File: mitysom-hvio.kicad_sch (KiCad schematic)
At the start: 34 parts, among them J1 Plug_Samtec_SEAM-50-02.0-L-08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, U1 TXS0102DQER, U48 TCA39306_VSSOP, U50 TCA39306_VSSOP, U501 TXU0304BQAR

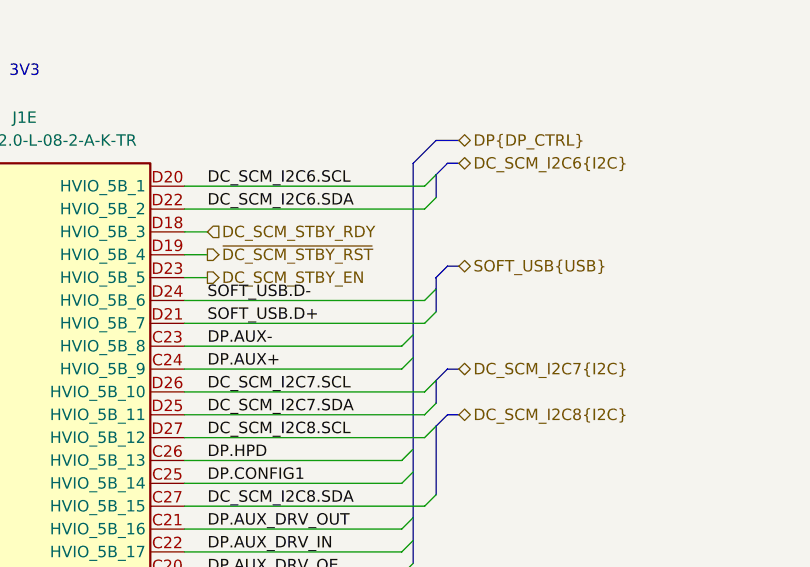
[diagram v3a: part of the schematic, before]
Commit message: [#100707] Connect power and low speed signals
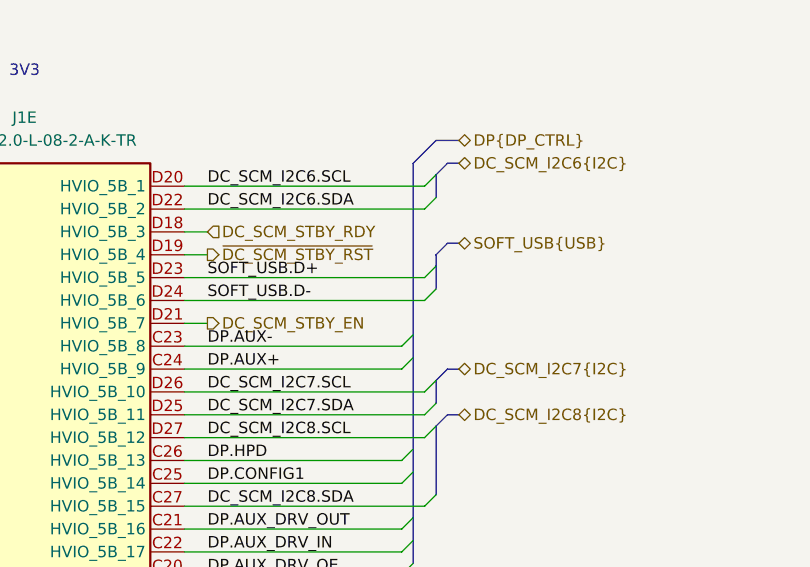
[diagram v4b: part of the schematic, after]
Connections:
- net DC_SCM_STBY_EN: now also J1.D21 (HVIO_5B_7); no longer J1.D23 (HVIO_5B_5)
- net SOFT_USB.D+: now also J1.D23 (HVIO_5B_5); no longer J1.D21 (HVIO_5B_7)
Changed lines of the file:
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@@
 	)
 	(bus_entry
+		(at 195.58 224.79)
+		(size -1.27 1.27)
+		(stroke
+			(width 0)
+			(type default)
+		)
+	)
+	(bus_entry
 		(at 210.82 102.87)
 		(size -1.27 -1.27)
@@
 	)
 	(bus_entry
-		(at 195.58 227.33)
-		(size -1.27 1.27)
-		(stroke
-			(width 0)
-			(type default)
-		)
-	)
-	(bus_entry
 		(at 238.76 179.07)
 		(size -1.27 1.27)
@@
 	)
 	(bus_entry
+		(at 195.58 222.25)
+		(size -1.27 1.27)
+		(stroke
+			(width 0)
+			(type default)
+		)
+	)
+	(bus_entry
 		(at 198.12 62.23)
 		(size -1.27 1.27)
@@
 	)
 	(bus_entry
-		(at 195.58 224.79)
-		(size -1.27 1.27)
-		(stroke
-			(width 0)
-			(type default)
-		)
-	)
-	(bus_entry
 		(at 92.71 257.81)
 		(size 1.27 1.27)
@@
 	(wire
 		(pts
-			(xy 167.64 228.6) (xy 194.31 228.6)
-		)
-		(stroke
-			(width 0)
-			(type default)
-		)
-	)
-	(wire
-		(pts
 			(xy 134.62 133.35) (xy 119.38 133.35)
 		)
@@
 	(bus
 		(pts
-			(xy 195.58 224.79) (xy 195.58 227.33)
-		)
-		(stroke
-			(width 0)
-			(type default)
-		)
-	)
-	(bus
-		(pts
 			(xy 104.14 95.25) (xy 104.14 97.79)
 		)
@@
 		)
 	)
+	(bus
+		(pts
+			(xy 198.12 219.71) (xy 196.85 219.71)
+		)
+		(stroke
+			(width 0)
+			(type default)
+		)
+	)
 	(wire
 		(pts
@@
 		)
 	)
+	(bus
+		(pts
+			(xy 195.58 220.98) (xy 195.58 222.25)
+		)
+		(stroke
+			(width 0)
+			(type default)
+		)
+	)
 	(wire
 		(pts
@@
 		)
 	)
-	(bus
-		(pts
-			(xy 198.12 222.25) (xy 196.85 222.25)
-		)
-		(stroke
-			(width 0)
-			(type default)
-		)
-	)
 	(wire
 		(pts
@@
 		)
 	)
-	(wire
+	(bus
 		(pts
-			(xy 170.18 223.52) (xy 167.64 223.52)
+			(xy 195.58 222.25) (xy 195.58 224.79)
 		)
 		(stroke
@@
 		)
 	)
-	(bus
-		(pts
-			(xy 195.58 223.52) (xy 195.58 224.79)
-		)
-		(stroke
-			(width 0)
-			(type default)
-		)
-	)
 	(wire
 		(pts
@@
 		)
 	)
+	(bus
+		(pts
+			(xy 196.85 219.71) (xy 195.58 220.98)
+		)
+		(stroke
+			(width 0)
+			(type default)
+		)
+	)
 	(wire
 		(pts
@@
 	(wire
 		(pts
+			(xy 167.64 223.52) (xy 194.31 223.52)
+		)
+		(stroke
+			(width 0)
+			(type default)
+		)
+	)
+	(wire
+		(pts
 			(xy 302.26 181.61) (xy 304.8 181.61)
 		)
@@
 	(bus
 		(pts
-			(xy 196.85 222.25) (xy 195.58 223.52)
-		)
-		(stroke
-			(width 0)
-			(type default)
-		)
-	)
-	(bus
-		(pts
 			(xy 91.44 256.54) (xy 92.71 257.81)
 		)
@@
 		)
 	)
+	(wire
+		(pts
+			(xy 170.18 228.6) (xy 167.64 228.6)
+		)
+		(stroke
+			(width 0)
+			(type default)
+		)
+	)
 	(label "DC_SCM_SPI_SCMCNTRL.~{CS0}"
 		(at 170.18 63.5 0)
@@
 		)
 	)
-	(label "SOFT_USB.D+"
-		(at 170.18 228.6 0)
-		(effects
-			(font
-				(size 1.27 1.27)
-			)
-			(justify left bottom)
-		)
-	)
 	(label "DC_SCM_NC-SI.CRS_DV"
 		(at 106.68 99.06 0)
@@
 		)
 	)
+	(label "SOFT_USB.D+"
+		(at 170.18 223.52 0)
+		(effects
+			(font
+				(size 1.27 1.27)
+			)
+			(justify left bottom)
+		)
+	)
 	(label "DC_SCM_ESPI.IO3"
 		(at 106.68 76.2 0)
@@
 		)
 	)
+	(hierarchical_label "DC_SCM_STBY_EN"
+		(shape output)
+		(at 170.18 228.6 0)
+		(effects
+			(font
+				(size 1.27 1.27)
+			)
+			(justify left)
+		)
+	)
 	(hierarchical_label "~{PECI_ALERT}"
 		(shape input)
@@
 		)
 	)
+	(hierarchical_label "SOFT_USB{USB}"
+		(shape bidirectional)
+		(at 198.12 219.71 0)
+		(effects
+			(font
+				(size 1.27 1.27)
+			)
+			(justify left)
+		)
+	)
 	(hierarchical_label "PCIE_RST_B"
 		(shape input)
@@
 		)
 	)
-	(hierarchical_label "SOFT_USB{USB}"
-		(shape bidirectional)
-		(at 198.12 222.25 0)
-		(effects
-			(font
-				(size 1.27 1.27)
-			)
-			(justify left)
-		)
-	)
 	(hierarchical_label "PCIE_PWR_EN"
 		(shape input)
@@
 		)
 	)
-	(hierarchical_label "DC_SCM_STBY_EN"
-		(shape output)
-		(at 170.18 223.52 0)
-		(effects
-			(font
-				(size 1.27 1.27)
-			)
-			(justify left)
-		)
-	)
 	(hierarchical_label "DC_SCM_SPI_SCMCNTRL{SPI}"
 		(shape bidirectional)
@@
 		(length 2.54)
 		(shape round)
-		(at 195.58 226.06 270)
+		(at 195.58 223.52 270)
 		(effects
 			(font
@@
 		)
 		(property "Netclass" "90Ohm-diff"
-			(at 199.39 226.06 0)
+			(at 199.39 223.52 0)
 			(show_name no)
 			(do_not_autoplace no)
@@
 		)
 		(property "Component Class" ""
-			(at 394.97 102.87 0)
+			(at 394.97 100.33 0)
 			(show_name no)
 			(do_not_autoplace no)

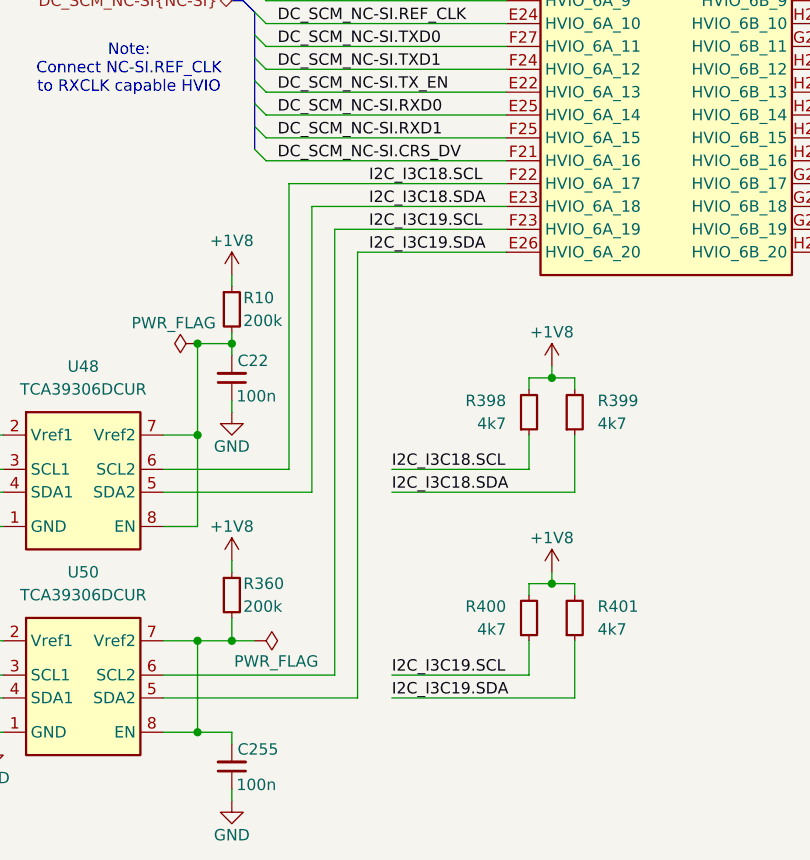
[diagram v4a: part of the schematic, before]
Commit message: [#101095] Swap I2C lines on HVIO
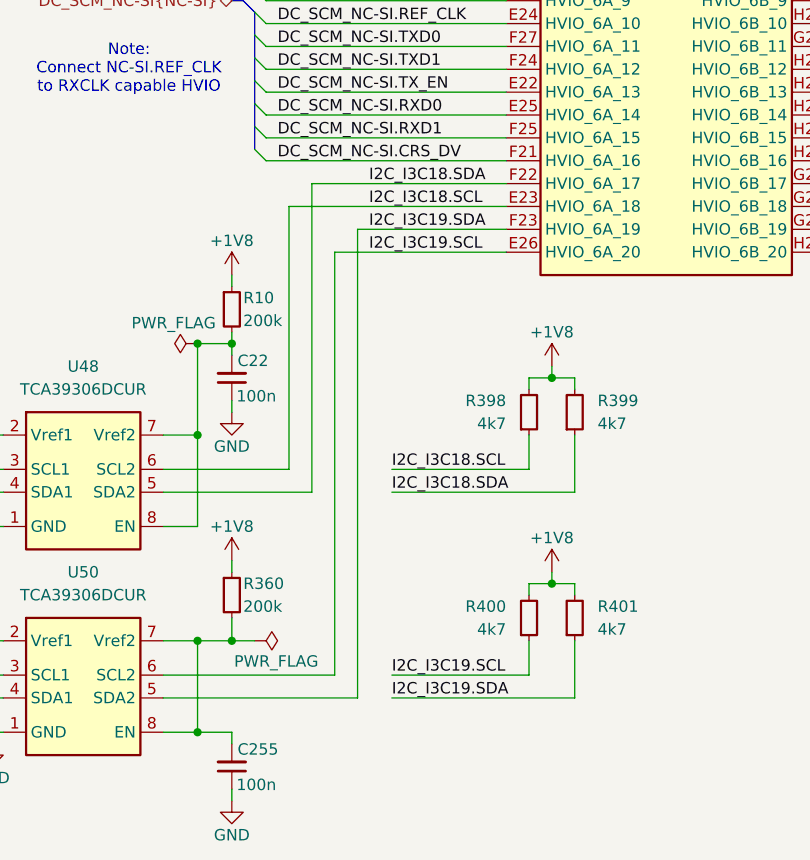
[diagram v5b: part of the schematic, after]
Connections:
- net I2C_I3C18.SCL: now also J1.E23 (HVIO_6A_18); no longer J1.F22 (HVIO_6A_17)
- net I2C_I3C18.SDA: now also J1.F22 (HVIO_6A_17); no longer J1.E23 (HVIO_6A_18)
- net I2C_I3C19.SCL: now also J1.E26 (HVIO_6A_20); no longer J1.F23 (HVIO_6A_19)
- net I2C_I3C19.SDA: now also J1.F23 (HVIO_6A_19); no longer J1.E26 (HVIO_6A_20)
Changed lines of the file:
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@@
 		)
 	)
-	(wire
-		(pts
-			(xy 110.49 104.14) (xy 132.08 104.14)
-		)
-		(stroke
-			(width 0)
-			(type default)
-		)
-	)
 	(bus
 		(pts
@@
 	(wire
 		(pts
+			(xy 110.49 101.6) (xy 110.49 135.89)
+		)
+		(stroke
+			(width 0)
+			(type default)
+		)
+	)
+	(wire
+		(pts
 			(xy 238.76 161.29) (xy 266.7 161.29)
 		)
@@
 	(wire
 		(pts
-			(xy 115.57 109.22) (xy 132.08 109.22)
+			(xy 113.03 109.22) (xy 132.08 109.22)
 		)
 		(stroke
@@
 	(wire
 		(pts
-			(xy 113.03 106.68) (xy 132.08 106.68)
+			(xy 115.57 106.68) (xy 132.08 106.68)
 		)
 		(stroke
@@
 	(wire
 		(pts
-			(xy 107.95 101.6) (xy 132.08 101.6)
-		)
-		(stroke
-			(width 0)
-			(type default)
-		)
-	)
-	(wire
-		(pts
 			(xy 167.64 88.9) (xy 209.55 88.9)
 		)
@@
 	(wire
 		(pts
-			(xy 110.49 104.14) (xy 110.49 135.89)
-		)
-		(stroke
-			(width 0)
-			(type default)
-		)
-	)
-	(wire
-		(pts
 			(xy 134.62 146.05) (xy 134.62 147.32)
 		)
@@
 	(wire
 		(pts
-			(xy 115.57 109.22) (xy 115.57 158.75)
-		)
-		(stroke
-			(width 0)
-			(type default)
-		)
-	)
-	(wire
-		(pts
 			(xy 302.26 179.07) (xy 304.8 179.07)
 		)
@@
 	(wire
 		(pts
+			(xy 113.03 156.21) (xy 113.03 109.22)
+		)
+		(stroke
+			(width 0)
+			(type default)
+		)
+	)
+	(wire
+		(pts
 			(xy 105.41 76.2) (xy 132.08 76.2)
 		)
@@
 	(wire
 		(pts
-			(xy 113.03 106.68) (xy 113.03 156.21)
-		)
-		(stroke
-			(width 0)
-			(type default)
-		)
-	)
-	(wire
-		(pts
 			(xy 93.98 261.62) (xy 132.08 261.62)
 		)
@@
 	(wire
 		(pts
+			(xy 115.57 106.68) (xy 115.57 158.75)
+		)
+		(stroke
+			(width 0)
+			(type default)
+		)
+	)
+	(wire
+		(pts
 			(xy 129.54 236.22) (xy 132.08 236.22)
 		)
@@
 	(wire
 		(pts
+			(xy 110.49 101.6) (xy 132.08 101.6)
+		)
+		(stroke
+			(width 0)
+			(type default)
+		)
+	)
+	(wire
+		(pts
 			(xy 238.76 146.05) (xy 266.7 146.05)
 		)
@@
 	(wire
 		(pts
-			(xy 107.95 101.6) (xy 107.95 133.35)
+			(xy 107.95 133.35) (xy 107.95 104.14)
 		)
 		(stroke
@@
 		)
 	)
+	(wire
+		(pts
+			(xy 107.95 104.14) (xy 132.08 104.14)
+		)
+		(stroke
+			(width 0)
+			(type default)
+		)
+	)
 	(bus
 		(pts
@@
 		)
 	)
+	(label "I2C_I3C18.SCL"
+		(at 116.84 104.14 0)
+		(effects
+			(font
+				(size 1.27 1.27)
+			)
+			(justify left bottom)
+		)
+	)
 	(label "DC_SCM_NC-SI.CRS_DV"
 		(at 106.68 99.06 0)
@@
 	)
 	(label "I2C_I3C19.SDA"
-		(at 116.84 109.22 0)
+		(at 119.38 158.75 0)
 		(effects
 			(font
@@
 		)
 	)
-	(label "I2C_I3C18.SDA"
-		(at 119.38 135.89 0)
-		(effects
-			(font
-				(size 1.27 1.27)
-			)
-			(justify left bottom)
-		)
-	)
-	(label "I2C_I3C18.SDA"
-		(at 116.84 104.14 0)
-		(effects
-			(font
-				(size 1.27 1.27)
-			)
-			(justify left bottom)
-		)
-	)
 	(label "GbE_TXD3"
 		(at 168.91 96.52 0)
@@
 		)
 	)
-	(label "I2C_I3C19.SCL"
-		(at 116.84 106.68 0)
-		(effects
-			(font
-				(size 1.27 1.27)
-			)
-			(justify left bottom)
-		)
-	)
 	(label "DC_SCM_NC-SI.RXD1"
 		(at 106.68 96.52 0)
@@
 		)
 	)
-	(label "I2C_I3C19.SCL"
-		(at 119.38 156.21 0)
-		(effects
-			(font
-				(size 1.27 1.27)
-			)
-			(justify left bottom)
-		)
-	)
 	(label "DP.CONFIG1"
 		(at 170.18 246.38 0)
@@
 		)
 	)
+	(label "I2C_I3C19.SDA"
+		(at 116.84 106.68 0)
+		(effects
+			(font
+				(size 1.27 1.27)
+			)
+			(justify left bottom)
+		)
+	)
 	(label "DC_SCM_I2C9.SDA"
 		(at 170.18 261.62 0)
@@
 		)
 	)
-	(label "I2C_I3C19.SDA"
-		(at 119.38 158.75 0)
+	(label "I2C_I3C18.SDA"
+		(at 116.84 101.6 0)
+		(effects
+			(font
+				(size 1.27 1.27)
+			)
+			(justify left bottom)
+		)
+	)
+	(label "I2C_I3C18.SCL"
+		(at 119.38 133.35 0)
+		(effects
+			(font
+				(size 1.27 1.27)
+			)
+			(justify left bottom)
+		)
+	)
+	(label "I2C_I3C18.SDA"
+		(at 119.38 135.89 0)
 		(effects
 			(font
@@
 		)
 	)
-	(label "I2C_I3C18.SCL"
-		(at 119.38 133.35 0)
-		(effects
-			(font
-				(size 1.27 1.27)
-			)
-			(justify left bottom)
-		)
-	)
 	(label "UART_1V8_TX"
 		(at 170.18 73.66 0)
@@
 		)
 	)
+	(label "I2C_I3C19.SCL"
+		(at 116.84 109.22 0)
+		(effects
+			(font
+				(size 1.27 1.27)
+			)
+			(justify left bottom)
+		)
+	)
 	(label "SOM.IO2"
 		(at 240.03 173.99 0)
@@
 		)
 	)
-	(label "I2C_I3C18.SCL"
-		(at 116.84 101.6 0)
-		(effects
-			(font
-				(size 1.27 1.27)
-			)
-			(justify left bottom)
-		)
-	)
 	(label "DC_SCM_NC-SI.REF_CLK"
 		(at 106.68 83.82 0)
@@
 		(effects
 			(font
+				(size 1.27 1.27)
+			)
+			(justify left bottom)
+		)
+	)
+	(label "I2C_I3C19.SCL"
+		(at 119.38 156.21 0)
+		(effects
+			(font

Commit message: [#101340] Update JTAG TRST divider
Re-use 10k/12k values from other sheets
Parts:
- R502: value R_1k_0402 -> R_10k_0402; symbol antmicroResistors0402:R_1k_0402 -> antmicroResistors0402:R_10k_0402; MPN CR0402-FX-1001GLF -> CR0402-FX-1002GLF; Val 1k -> 10k
- R503: value R_1k2_0402 -> R_12k_0402; symbol antmicroResistors0402:R_1k2_0402 -> antmicroResistors0402:R_12k_0402; MPN CR0402-FX-1201GLF -> CR0402-FX-1202GLF; Val 1k2 -> 12k
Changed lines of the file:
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@@
 	)
 	(symbol
-		(lib_id "antmicroResistors0402:R_1k2_0402")
+		(lib_id "antmicroResistors0402:R_12k_0402")
 		(at 344.17 157.48 90)
 		(unit 1)
@@
 			)
 		)
-		(property "Value" "R_1k2_0402"
+		(property "Value" "R_12k_0402"
 			(at 356.87 137.16 0)
 			(hide yes)
@@
 			)
 		)
-		(property "Description" "SMD Chip Resistor, 1.2 kohm, ± 1%, 62.5 mW, 0402 [1005 Metric], Thick Film, General Purpose"
+		(property "Description" "SMD Chip Resistor, 12 kohm, ± 1%, 62.5 mW, 0402 [1005 Metric], Thick Film, General Purpose"
 			(at 374.65 137.16 0)
 			(hide yes)
@@
 			)
 		)
-		(property "MPN" "CR0402-FX-1201GLF"
+		(property "MPN" "CR0402-FX-1202GLF"
 			(at 364.49 137.16 0)
 			(hide yes)
@@
 			)
 		)
-		(property "Val" "1k2"
+		(property "Val" "12k"
 			(at 346.71 156.21 90)
 			(show_name no)
@@
 	)
 	(symbol
-		(lib_id "antmicroResistors0402:R_1k_0402")
+		(lib_id "antmicroResistors0402:R_10k_0402")
 		(at 344.17 149.86 90)
 		(unit 1)
@@
 			)
 		)
-		(property "Value" "R_1k_0402"
+		(property "Value" "R_10k_0402"
 			(at 356.87 129.54 0)
 			(hide yes)
@@
 			)
 		)
-		(property "Description" "SMD Chip Resistor, 1 kohm, ± 1%, 63 mW, 0402 [1005 Metric], Thick Film, General Purpose"
+		(property "Description" "SMD Chip Resistor, 10 kohm, ± 1%, 62.5 mW, 0402 [1005 Metric], Thick Film, General Purpose"
 			(at 374.65 129.54 0)
 			(hide yes)
@@
 			)
 		)
-		(property "MPN" "CR0402-FX-1001GLF"
+		(property "MPN" "CR0402-FX-1002GLF"
 			(at 364.49 129.54 0)
 			(hide yes)
@@
 			)
 		)
-		(property "Val" "1k"
+		(property "Val" "10k"
 			(at 346.71 148.59 90)
 			(show_name no)

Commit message: [#101340] Update date on SCH and PCB
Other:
- note added: "TXS0102 has internal pullup resistors"
- note removed: "TXS0102 has interal pullup resistors"
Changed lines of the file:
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@@
 	(title_block
 		(title "altera-modular-agilex-5-dc-scm")
-		(date "2026-07-13")
+		(date "2026-07-24")
 		(rev "1.0.0")
 		(company "Altera")
@@
 		)
 	)
-	(text "TXS0102 has\ninteral pullup resistors"
+	(text "TXS0102 has\ninternal pullup resistors"
 		(exclude_from_sim no)
 		(at 256.54 87.63 0)
